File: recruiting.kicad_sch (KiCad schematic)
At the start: 19 parts, among them Q1 IRF9383M, Q2 IRF9383M

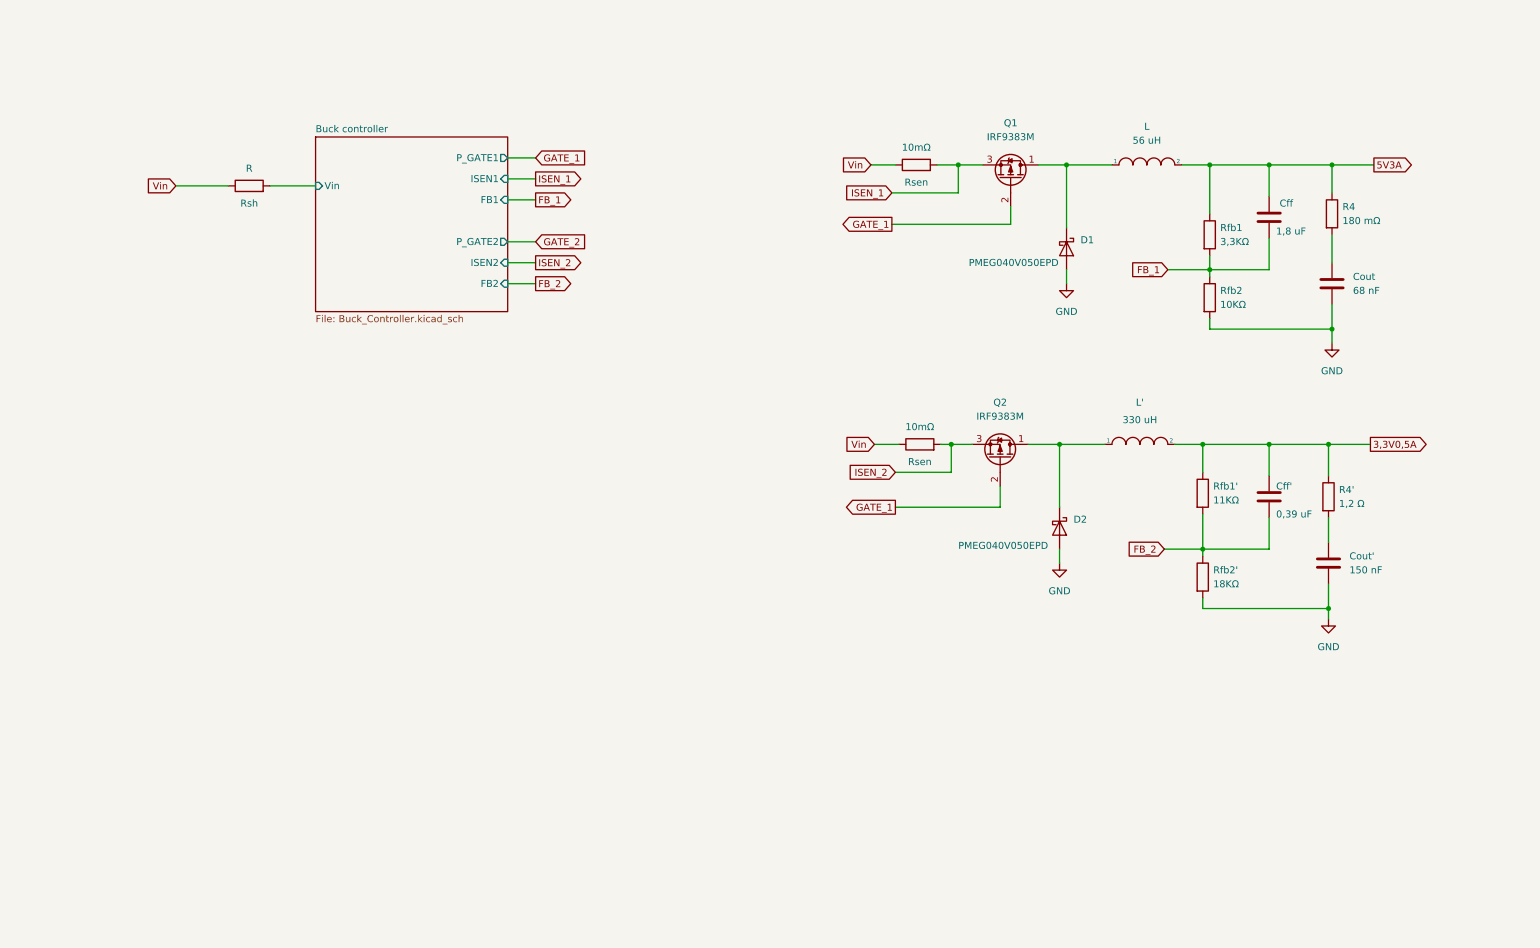
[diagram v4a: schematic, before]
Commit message: alcune modifiche ai package di alcuni componenti e continuazione del design del circuito stampato
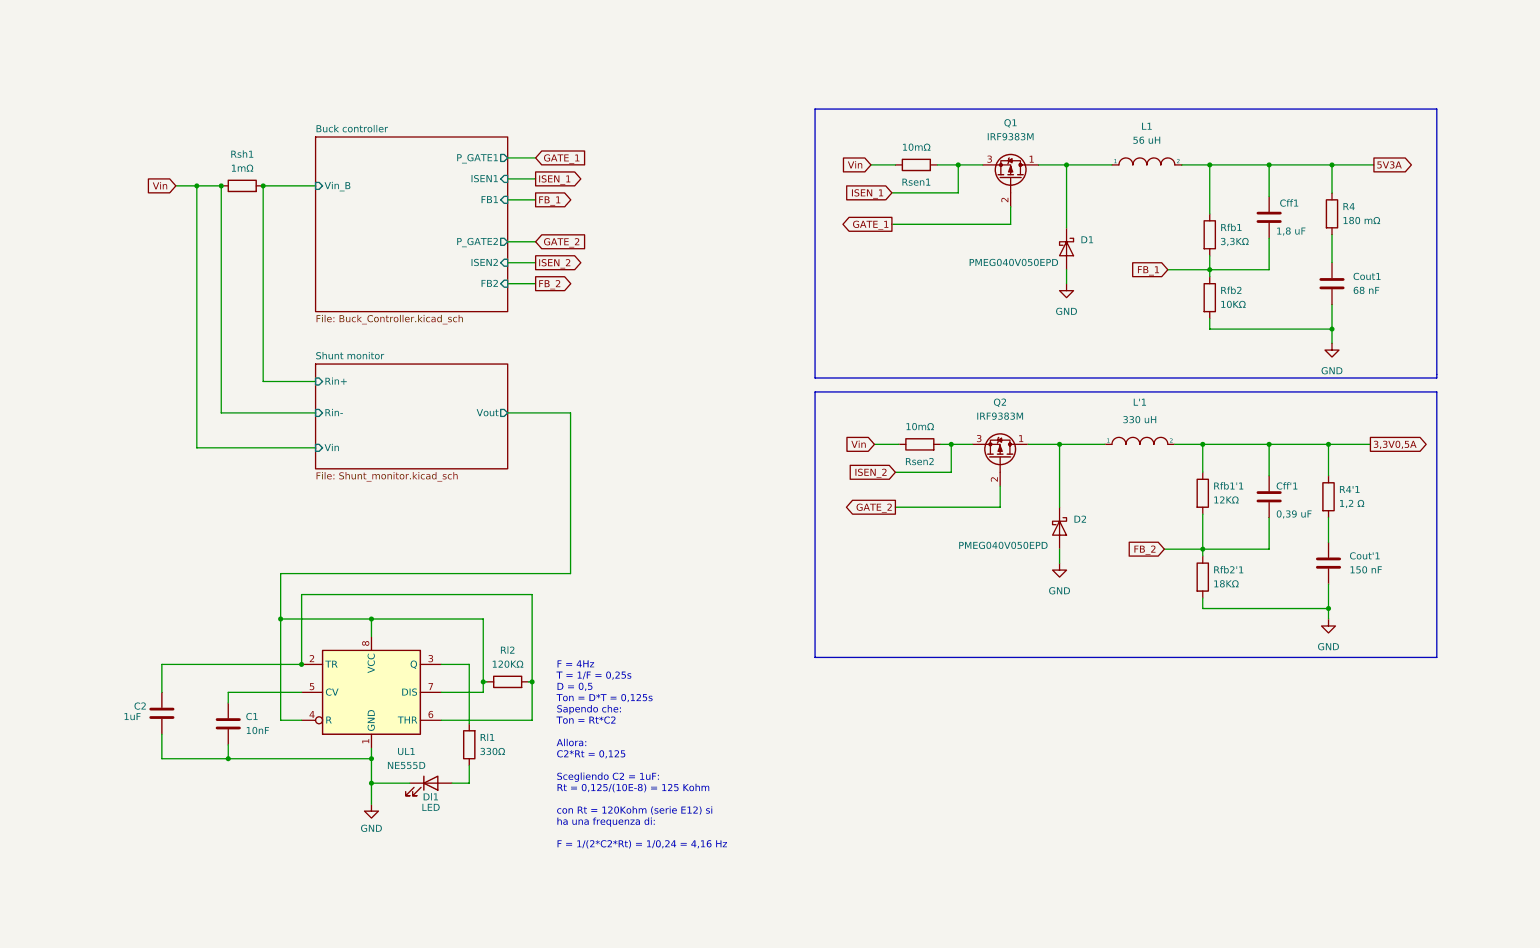
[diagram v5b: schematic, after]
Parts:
- removed Rsh: R, symbol Device:R
- added C1: 10nF, Capacitor_SMD:C_0603_1608Metric, symbol Device:C
- added C2: 1uF, Capacitor_SMD:C_0603_1608Metric, symbol Device:C
- added Dl1: LED, Diode_SMD:D_0805_2012Metric, symbol Device:LED
- added Rl1: 330Ω, Resistor_SMD:R_0402_1005Metric, symbol Device:R
- added Rl2: 120KΩ, Resistor_SMD:R_0402_1005Metric, symbol Device:R
- added Rsh1: 1mΩ, Resistor_SMD:R_0805_2012Metric, symbol Device:R
- added UL1: NE555D, Package_SO:SOIC-8_3.9x4.9mm_P1.27mm, symbol Timer:NE555D
- Cff'1: renamed from Cff'; footprint (none) -> Capacitor_SMD:C_0603_1608Metric
- Cff1: renamed from Cff; footprint (none) -> Capacitor_SMD:C_0603_1608Metric
- Cout'1: renamed from Cout'; footprint (none) -> Capacitor_SMD:C_1206_3216Metric
- Cout1: renamed from Cout; footprint (none) -> Capacitor_SMD:C_1206_3216Metric
- L'1: renamed from L'; footprint (none) -> Inductor_SMD:L_Wuerth_HCI-2212
- L1: renamed from L; footprint (none) -> Inductor_SMD:L_Pulse_PA4344
- R4: footprint Resistor_SMD:R_1210_3225Metric -> Resistor_SMD:R_0805_2012Metric
- R4'1: renamed from R4'; footprint Resistor_SMD:R_1210_3225Metric -> Resistor_SMD:R_0805_2012Metric
- Rfb1, Rfb2: footprint Resistor_SMD:R_1210_3225Metric -> Resistor_SMD:R_0603_1608Metric
- Rfb1'1: renamed from Rfb1'; value 11KΩ -> 12KΩ; footprint Resistor_SMD:R_1210_3225Metric -> Resistor_SMD:R_0603_1608Metric
- Rfb2'1: renamed from Rfb2'; footprint Resistor_SMD:R_1210_3225Metric -> Resistor_SMD:R_0603_1608Metric
- Rsen1, Rsen2: renamed from Rsen; footprint (none) -> Resistor_SMD:R_0805_2012Metric
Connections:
- net GATE_1: no longer Q2.2 (G)
- net GATE_2: now also Q2.2 (G)
- net GND: now also C1.1, C2.1, Dl1.1 (K), UL1.1 (GND)
- net Vin: now also Rsh1.1
- new net: Dl1.2 (A), Rl1.1
- new net: C1.2, UL1.5 (CV)
- new net: C2.2, Rl2.2, UL1.2 (TR), UL1.6 (THR)
- new net: Rl1.2, UL1.3 (Q)
- new net Buck controller/Vin_B: Rsh1.2
- new net Shunt monitor/Vout: Rl2.1, UL1.4 (R), UL1.7 (DIS), UL1.8 (VCC)
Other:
- added sheet Shunt monitor (Shunt_monitor.kicad_sch)
- sheet Buck controller ports: added Vin_B; removed Vin
- note added: "F = 4Hz T = 1/F = 0,25s D = 0,5 Ton = D*T = 0,125s Sapendo che: Ton = Rt*C2 Allora: C2*Rt = 0,125 Scegliendo C2 = 1uF: Rt = 0,125/(10E-8) = 125 Kohm con Rt = 120Kohm (serie E12) si ha una frequenza di: F = 1/(2*C2*Rt) = 1/0,24 = 4,16 Hz"

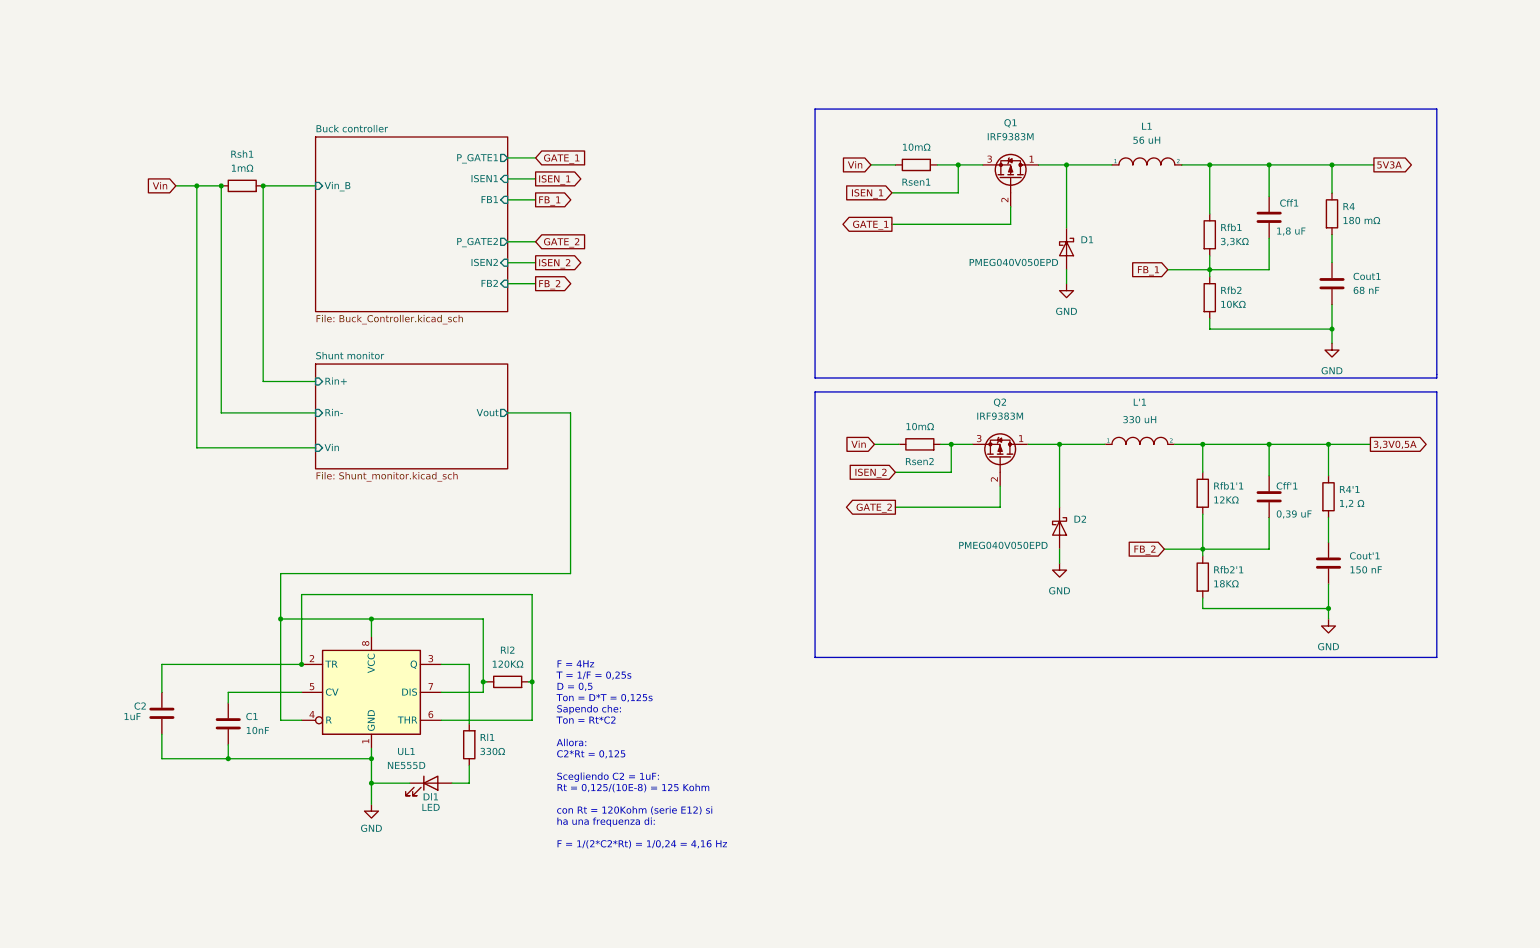
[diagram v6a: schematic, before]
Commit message: modificalo lo schematic e rifatto in parte il design PCB
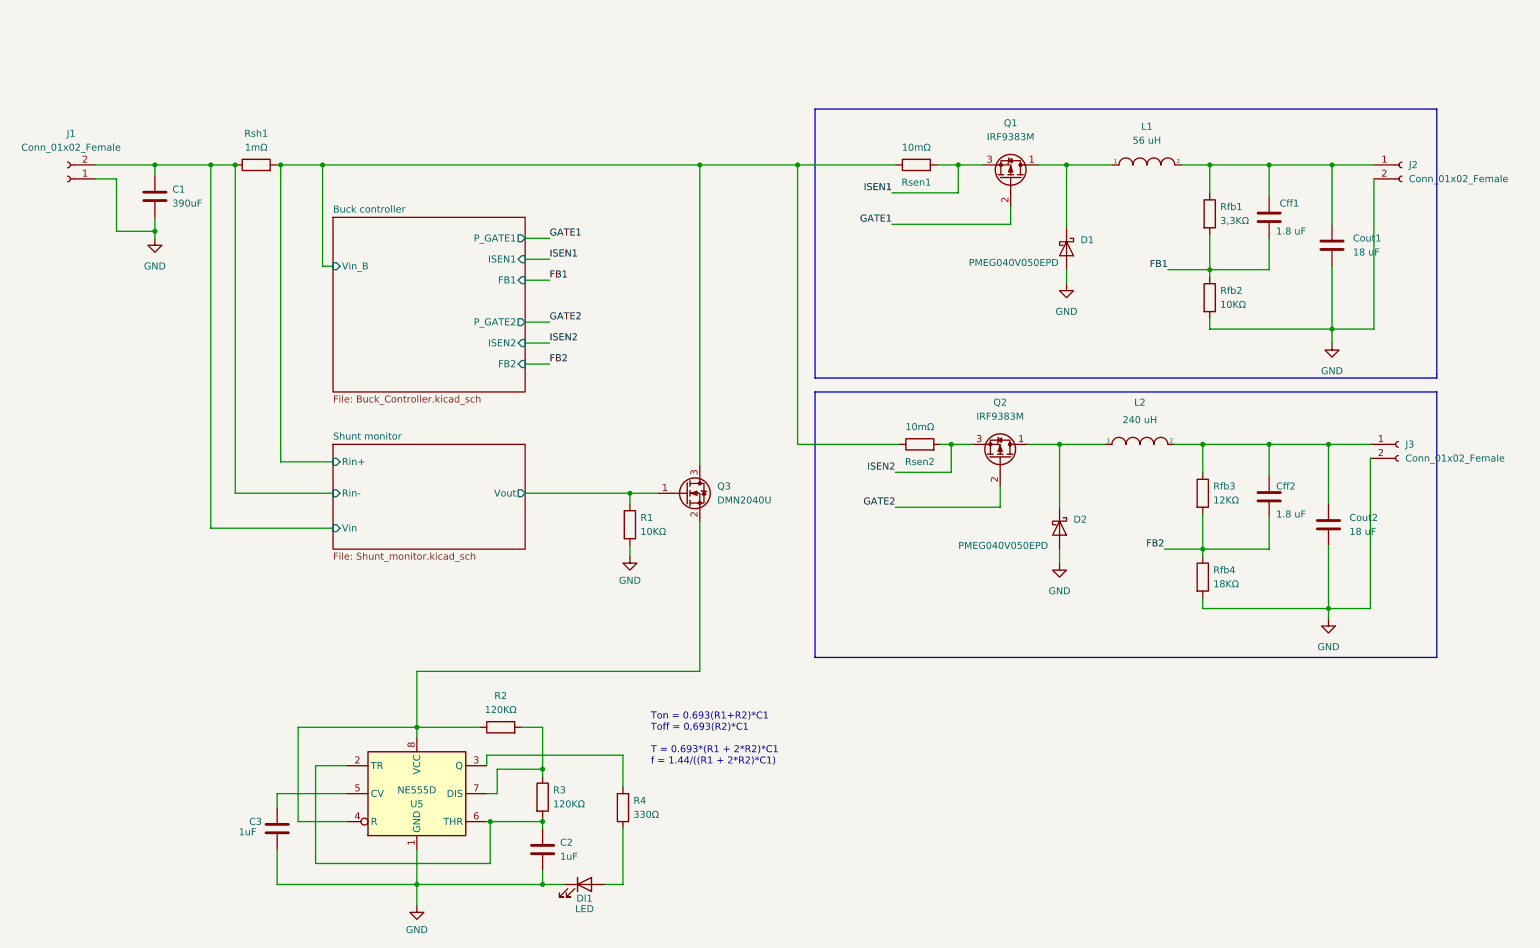
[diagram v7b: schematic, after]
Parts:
- removed R4: 180 mΩ, Resistor_SMD:R_0805_2012Metric, symbol Device:R
- removed R4'1: 1,2 Ω, Resistor_SMD:R_0805_2012Metric, symbol Device:R
- added C1: 390uF, Capacitor_SMD:C_1206_3216Metric, symbol Device:C
- added J1, J2, J3: Conn_01x02_Female, Connector_JST:JST_NV_B02P-NV_1x02_P5.00mm_Vertical, symbol Connector:Conn_01x02_Female
- added Q3: DMN2040U, Package_TO_SOT_SMD:SOT-23, symbol Transistor_FET:DMN2041L
- added R1: 10KΩ, Resistor_SMD:R_0402_1005Metric, symbol Device:R
- added R2: 120KΩ, Resistor_SMD:R_0402_1005Metric, symbol Device:R
- C2: renamed from C1; value 10nF -> 1uF
- Cff1: value 1,8 uF -> 1.8 uF
- Cff2: renamed from Cff'1; value 0,39 uF -> 1.8 uF
- Cout1: value 68 nF -> 18 uF
- Cout2: renamed from Cout'1; value 150 nF -> 18 uF
- L2: renamed from L'1; value 330 uH -> 240 uH
- renumbered C2 to C3, Rl2 to R3, Rl1 to R4, Rfb1'1 to Rfb3, Rfb2'1 to Rfb4, UL1 to U5
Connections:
- net 3,3V0,5A is gone; now on an unnamed net: Cff2.1, L2.2, Rfb3.1
- net 5V3A is gone; now on an unnamed net: Cff1.1, L1.2, Rfb1.1
- net Buck controller/Vin_B: now also Rsen1.1, Rsen2.1, Q3.3 (D)
- net GND: now also C1.2, J1.1 (Pin_1), J2.2 (Pin_2), J3.2 (Pin_2), R1.2
- net Shunt monitor/Vout: now also Q3.1 (G), R1.1; no longer R3.1, U5.4 (R), U5.7 (DIS), U5.8 (VCC)
- net at Cout1.1: now also J2.1 (Pin_1)
- net at C2.2: now also R3.2, U5.2 (TR), U5.6 (THR); no longer U5.5 (CV)
- net at Cout2.1: now also J3.1 (Pin_1)
- net FB_1 renamed FB1
- net FB_2 renamed FB2
- net GATE_1 renamed GATE1
- net GATE_2 renamed GATE2
- net ISEN_1 renamed ISEN1
- net ISEN_2 renamed ISEN2
- removed net Vin: Rsen1.1, Rsen2.1, Rsh1.1
- new net: Q3.2 (S), R2.1, U5.4 (R), U5.8 (VCC)
- new net: R2.2, R3.1, U5.7 (DIS)
- new net: C3.2, U5.5 (CV)
- new net Shunt monitor/Rin-: C1.1, J1.2 (Pin_2), Rsh1.1
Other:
- note added: "Ton = 0.693(R1+R2)*C1 Toff = 0,693(R2)*C1 T = 0.693*(R1 + 2*R2)*C1 f = 1.44/((R1 + 2*R2)*C1)"
- note removed: "F = 4Hz T = 1/F = 0,25s D = 0,5 Ton = D*T = 0,125s Sapendo che: Ton = Rt*C2 Allora: C2*Rt = 0,125 Scegliendo C2 = 1uF: Rt = 0,125/(10E-8) = 125 Kohm con Rt = 120Kohm (serie E12) si ha una frequenza di: F = 1/(2*C2*Rt) = 1/0,24 = 4,16 Hz"
- moved on the sheet: C2, C3, Cout1, Cout2, Dl1, R3, R4, Rfb1, Rsh1, U5
